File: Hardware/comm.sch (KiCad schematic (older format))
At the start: 0 parts

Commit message: reassigned pin to correct I2C1, I2C2, and USART1 connections
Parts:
- added C?: CP_Small, symbol CP_Small
- added P?: CONN_01X06, symbol CONN_01X06
- added P?: GROVE_OUTPUT_2MM, symbol CONN_01X04
- added P?: GROVE_INPUT_2MM, symbol CONN_01X04
- added P?: BOOT, symbol CONN_01X03
- added R? (x5): 0, symbol R_Small
- added SW?: SW_Push, symbol SW_Push
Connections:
- net labels added: BOOT0, GND, NRST, PWR, SCL, SDA, SWCLK, SWDIO, TRACE
- wire segments 0 -> 31
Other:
- note added: "NOTE: TRACE is reserved and not connected"
- note added: "RESET BUTTON"

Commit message: initial footprint assignments
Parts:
- removed C?: CP_Small, symbol CP_Small
- added C301: 0.1u, Capacitors_SMD:C_0805, symbol C_Small
- P301: renamed from P?; footprint (none) -> Pin_Headers:Pin_Header_Straight_1x06
- P304: renamed from P?; footprint (none) -> Pin_Headers:Pin_Header_Straight_1x03
- R301, R302, R303, R304, R305: renamed from R?; footprint (none) -> Resistors_SMD:R_0805
- gave numbers to parts that had none: 3
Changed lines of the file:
@@
 $EndDescr
 $Comp
-L CONN_01X06 P?
+L CONN_01X06 P301
 U 1 1 58DF9C44
 P 4515 1295
-F 0 "P?" H 4515 1645 50  0000 C CNN
+F 0 "P301" H 4515 1645 50  0000 C CNN
 F 1 "CONN_01X06" V 4615 1295 50  0000 C CNN
-F 2 "" H 4515 1295 50  0000 C CNN
+F 2 "Pin_Headers:Pin_Header_Straight_1x06" H 4515 1295 50  0001 C CNN
 F 3 "" H 4515 1295 50  0000 C CNN
 	1    4515 1295
@@
 $EndComp
 $Comp
-L R_Small R?
+L R_Small R301
 U 1 1 58DF9D23
 P 4085 1045
-F 0 "R?" H 4115 1065 50  0000 L CNN
+F 0 "R301" H 4115 1065 50  0000 L CNN
 F 1 "0" H 4115 1005 50  0000 L CNN
-F 2 "" H 4085 1045 50  0000 C CNN
+F 2 "Resistors_SMD:R_0805" H 4085 1045 50  0001 C CNN
 F 3 "" H 4085 1045 50  0000 C CNN
 F 4 "Value" H 4085 1045 60  0001 C CNN "Fieldname"
@@
 SWCLK
 $Comp
-L GND #PWR?
+L GND #PWR020
 U 1 1 58DF9E37
 P 2955 1245
-F 0 "#PWR?" H 2955 995 50  0001 C CNN
+F 0 "#PWR020" H 2955 995 50  0001 C CNN
 F 1 "GND" H 2955 1095 50  0000 C CNN
 F 2 "" H 2955 1245 50  0000 C CNN
@@
 NOTE: TRACE is reserved and not connected
 $Comp
-L CONN_01X04 P?
+L CONN_01X04 P302
 U 1 1 58E0FECE
 P 7910 1290
-F 0 "P?" H 7910 1540 50  0000 C CNN
+F 0 "P302" H 7910 1540 50  0000 C CNN
 F 1 "GROVE_OUTPUT_2MM" V 8010 1290 50  0000 C CNN
-F 2 "" H 7910 1290 50  0000 C CNN
+F 2 "" H 7910 1290 50  0001 C CNN
 F 3 "" H 7910 1290 50  0000 C CNN
 F 4 "Value" H 7910 1290 60  0001 C CNN "Fieldname"
@@
 PWR
 $Comp
-L GND #PWR?
+L GND #PWR021
 U 1 1 58E10BA0
 P 6750 1140
-F 0 "#PWR?" H 6750 890 50  0001 C CNN
+F 0 "#PWR021" H 6750 890 50  0001 C CNN
 F 1 "GND" H 6750 990 50  0000 C CNN
 F 2 "" H 6750 1140 50  0000 C CNN
@@
 SDA
 $Comp
-L CONN_01X04 P?
+L CONN_01X04 P303
 U 1 1 58E10C1E
 P 7910 2220
-F 0 "P?" H 7910 2470 50  0000 C CNN
+F 0 "P303" H 7910 2470 50  0000 C CNN
 F 1 "GROVE_INPUT_2MM" V 8010 2220 50  0000 C CNN
-F 2 "" H 7910 2220 50  0000 C CNN
+F 2 "" H 7910 2220 50  0001 C CNN
 F 3 "" H 7910 2220 50  0000 C CNN
 F 4 "Value" H 7910 2220 60  0001 C CNN "Fieldname"
@@
 $EndComp
 $Comp
-L R_Small R?
+L R_Small R305
 U 1 1 58E10C90
 P 7640 1760
-F 0 "R?" H 7670 1780 50  0000 L CNN
+F 0 "R305" H 7670 1780 50  0000 L CNN
 F 1 "0" H 7615 1765 50  0000 L CNN
-F 2 "" H 7640 1760 50  0000 C CNN
+F 2 "Resistors_SMD:R_0805" H 7640 1760 50  0001 C CNN
 F 3 "" H 7640 1760 50  0000 C CNN
 F 4 "Value" H 7640 1760 60  0001 C CNN "Fieldname"
@@
 $EndComp
 $Comp
-L R_Small R?
+L R_Small R304
 U 1 1 58E10CC8
 P 7550 1760
-F 0 "R?" H 7555 1875 50  0000 L CNN
+F 0 "R304" H 7555 1875 50  0000 L CNN
 F 1 "0" H 7530 1760 50  0000 L CNN
-F 2 "" H 7550 1760 50  0000 C CNN
+F 2 "Resistors_SMD:R_0805" H 7550 1760 50  0001 C CNN
 F 3 "" H 7550 1760 50  0000 C CNN
 F 4 "Value" H 7550 1760 60  0001 C CNN "Fieldname"
@@
 $EndComp
 $Comp
-L R_Small R?
+L R_Small R303
 U 1 1 58E10CF9
 P 7450 1760
-F 0 "R?" H 7455 1880 50  0000 L CNN
+F 0 "R303" H 7455 1880 50  0000 L CNN
 F 1 "0" H 7430 1760 50  0000 L CNN
-F 2 "" H 7450 1760 50  0000 C CNN
+F 2 "Resistors_SMD:R_0805" H 7450 1760 50  0001 C CNN
 F 3 "" H 7450 1760 50  0000 C CNN
 F 4 "Value" H 7450 1760 60  0001 C CNN "Fieldname"
@@
 $EndComp
 $Comp
-L R_Small R?
+L R_Small R302
 U 1 1 58E10D31
 P 7350 1760
-F 0 "R?" H 7200 1795 50  0000 L CNN
+F 0 "R302" H 7200 1795 50  0000 L CNN
 F 1 "0" H 7330 1760 50  0000 L CNN
-F 2 "" H 7350 1760 50  0000 C CNN
+F 2 "Resistors_SMD:R_0805" H 7350 1760 50  0001 C CNN
 F 3 "" H 7350 1760 50  0000 C CNN
 F 4 "Value" H 7350 1760 60  0001 C CNN "Fieldname"
@@
 $EndComp
 $Comp
-L SW_Push SW?
+L SW_Push SW301
 U 1 1 58E13285
 P 5620 3800
-F 0 "SW?" H 5670 3900 50  0000 L CNN
+F 0 "SW301" H 5670 3900 50  0000 L CNN
 F 1 "SW_Push" H 5620 3740 50  0000 C CNN
-F 2 "" H 5620 4000 50  0000 C CNN
+F 2 "" H 5620 4000 50  0001 C CNN
 F 3 "" H 5620 4000 50  0000 C CNN
 	1    5620 3800
@@
 $EndComp
 $Comp
-L CP_Small C?
-U 1 1 58E132D2
-P 5625 4050
-F 0 "C?" H 5635 4120 50  0000 L CNN
-F 1 "CP_Small" H 5635 3970 50  0000 L CNN
-F 2 "" H 5625 4050 50  0000 C CNN
-F 3 "" H 5625 4050 50  0000 C CNN
-	1    5625 4050
-	0    1    1    0
-$EndComp
-$Comp
-L GND #PWR?
+L GND #PWR022
 U 1 1 58E1344F
 P 5820 4145
-F 0 "#PWR?" H 5820 3895 50  0001 C CNN
+F 0 "#PWR022" H 5820 3895 50  0001 C CNN
 F 1 "GND" H 5820 3995 50  0000 C CNN
 F 2 "" H 5820 4145 50  0000 C CNN
@@
 RESET BUTTON
 $Comp
-L CONN_01X03 P?
+L CONN_01X03 P304
 U 1 1 58E182A5
 P 9270 4480
-F 0 "P?" H 9270 4680 50  0000 C CNN
+F 0 "P304" H 9270 4680 50  0000 C CNN
 F 1 "BOOT" V 9370 4480 50  0000 C CNN
-F 2 "" H 9270 4480 50  0000 C CNN
+F 2 "Pin_Headers:Pin_Header_Straight_1x03" H 9270 4480 50  0001 C CNN
 F 3 "" H 9270 4480 50  0000 C CNN
 F 4 "Value" H 9270 4480 60  0001 C CNN "Fieldname"
@@
 PWR
 $Comp
-L GND #PWR?
+L GND #PWR023
 U 1 1 58E18682
 P 8540 4580
-F 0 "#PWR?" H 8540 4330 50  0001 C CNN
+F 0 "#PWR023" H 8540 4330 50  0001 C CNN
 F 1 "GND" H 8540 4430 50  0000 C CNN
 F 2 "" H 8540 4580 50  0000 C CNN
@@
 Text HLabel 8540 4480 0    60   Input ~ 0
 BOOT0
+$Comp
+L C_Small C301
+U 1 1 58E1A7F8
+P 5625 4050
+F 0 "C301" H 5635 4120 50  0000 L CNN
+F 1 "0.1u" H 5635 3970 50  0000 L CNN
+F 2 "Capacitors_SMD:C_0805" H 5625 4050 50  0001 C CNN
+F 3 "" H 5625 4050 50  0000 C CNN
+F 4 "Value" H 5625 4050 60  0001 C CNN "Fieldname"
+	1    5625 4050
+	0    1    1    0
+$EndComp
 $EndSCHEMATC

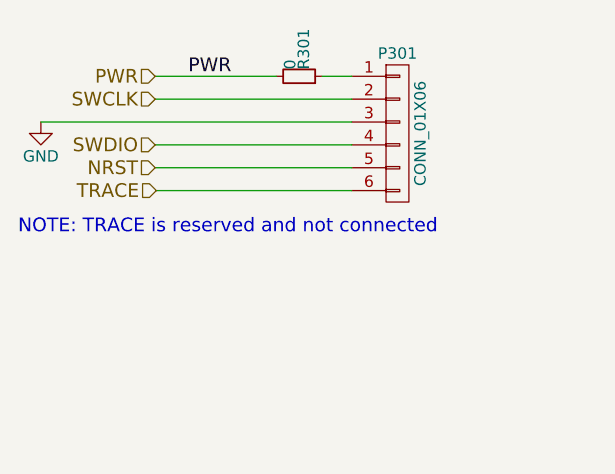
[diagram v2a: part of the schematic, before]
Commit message: added crystal details and usb footprint
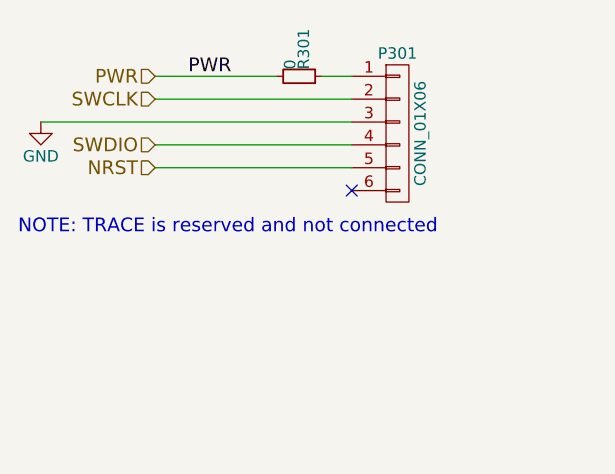
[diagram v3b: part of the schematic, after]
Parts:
- P302, P303: footprint (none) -> Connectors_JST:JST_PH_B4B-PH-K_04x2.00mm_Straight
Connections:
- net TRACE: no longer names the net of P301.6 (P6)
- no-connect marks 0 -> 1
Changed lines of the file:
@@
 SWCLK
 $Comp
-L GND #PWR020
+L GND #PWR022
 U 1 1 58DF9E37
 P 2955 1245
-F 0 "#PWR020" H 2955 995 50  0001 C CNN
+F 0 "#PWR022" H 2955 995 50  0001 C CNN
 F 1 "GND" H 2955 1095 50  0000 C CNN
 F 2 "" H 2955 1245 50  0000 C CNN
@@
 Text HLabel 3455 1445 0    60   Input ~ 0
 NRST
-Text HLabel 3460 1545 0    60   Input ~ 0
-TRACE
 Text Notes 2855 1740 0    60   ~ 0
 NOTE: TRACE is reserved and not connected
@@
 F 0 "P302" H 7910 1540 50  0000 C CNN
 F 1 "GROVE_OUTPUT_2MM" V 8010 1290 50  0000 C CNN
-F 2 "" H 7910 1290 50  0001 C CNN
+F 2 "Connectors_JST:JST_PH_B4B-PH-K_04x2.00mm_Straight" H 7910 1290 50  0001 C CNN
 F 3 "" H 7910 1290 50  0000 C CNN
 F 4 "Value" H 7910 1290 60  0001 C CNN "Fieldname"
@@
 PWR
 $Comp
-L GND #PWR021
+L GND #PWR023
 U 1 1 58E10BA0
 P 6750 1140
-F 0 "#PWR021" H 6750 890 50  0001 C CNN
+F 0 "#PWR023" H 6750 890 50  0001 C CNN
 F 1 "GND" H 6750 990 50  0000 C CNN
 F 2 "" H 6750 1140 50  0000 C CNN
@@
 F 0 "P303" H 7910 2470 50  0000 C CNN
 F 1 "GROVE_INPUT_2MM" V 8010 2220 50  0000 C CNN
-F 2 "" H 7910 2220 50  0001 C CNN
+F 2 "Connectors_JST:JST_PH_B4B-PH-K_04x2.00mm_Straight" H 7910 2220 50  0001 C CNN
 F 3 "" H 7910 2220 50  0000 C CNN
 F 4 "Value" H 7910 2220 60  0001 C CNN "Fieldname"
@@
 $EndComp
 $Comp
-L GND #PWR022
+L GND #PWR024
 U 1 1 58E1344F
 P 5820 4145
-F 0 "#PWR022" H 5820 3895 50  0001 C CNN
+F 0 "#PWR024" H 5820 3895 50  0001 C CNN
 F 1 "GND" H 5820 3995 50  0000 C CNN
 F 2 "" H 5820 4145 50  0000 C CNN
@@
 	4315 1345 3455 1345
 Wire Wire Line
-	4315 1545 3460 1545
-Wire Wire Line
 	6750 1140 7710 1140
 Wire Wire Line
@@
 PWR
 $Comp
-L GND #PWR023
+L GND #PWR025
 U 1 1 58E18682
 P 8540 4580
-F 0 "#PWR023" H 8540 4330 50  0001 C CNN
+F 0 "#PWR025" H 8540 4330 50  0001 C CNN
 F 1 "GND" H 8540 4430 50  0000 C CNN
 F 2 "" H 8540 4580 50  0000 C CNN
@@
 	0    1    1    0
 $EndComp
+NoConn ~ 4315 1545
 $EndSCHEMATC

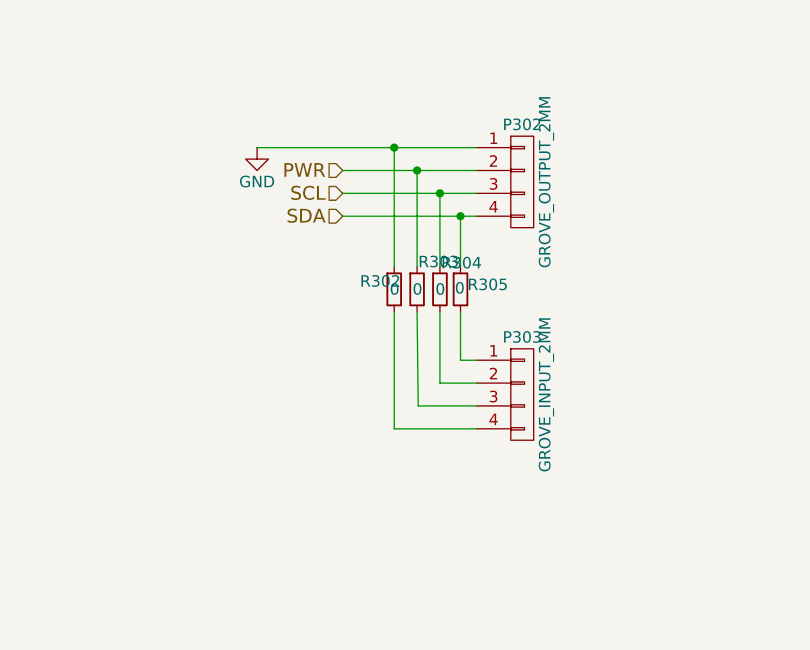
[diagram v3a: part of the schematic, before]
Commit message: changed grove connectors to jst sh and added VCC and GND to other headers
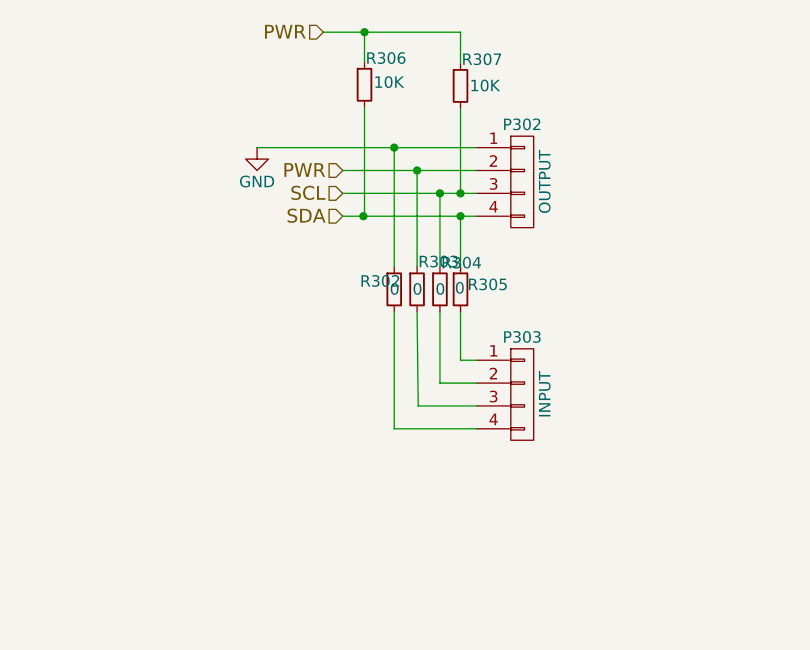
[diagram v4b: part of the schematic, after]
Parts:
- added R306, R307: 10K, Resistors_SMD:R_0805, symbol R_Small
- P302: value GROVE_OUTPUT_2MM -> OUTPUT; footprint Connectors_JST:JST_PH_B4B-PH-K_04x2.00mm_Straight -> Connectors_JST:JST_SH_BM04B-SRSS-TB_04x1.00mm_Straight; Fieldname Value -> (none); MPN (none) -> BM04B-SRSS-TB(LF)(SN)
- P303: value GROVE_INPUT_2MM -> INPUT; footprint Connectors_JST:JST_PH_B4B-PH-K_04x2.00mm_Straight -> Connectors_JST:JST_SH_BM04B-SRSS-TB_04x1.00mm_Straight; MPN (none) -> BM04B-SRSS-TB(LF)(SN)
- SW301: MPN (none) -> TL3315NF100Q
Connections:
- net PWR: now also R306.1, R307.1
- net SCL: now also R307.2
- net SDA: now also R306.2
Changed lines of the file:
@@
 SWCLK
 $Comp
-L GND #PWR022
+L GND #PWR019
 U 1 1 58DF9E37
 P 2955 1245
-F 0 "#PWR022" H 2955 995 50  0001 C CNN
+F 0 "#PWR019" H 2955 995 50  0001 C CNN
 F 1 "GND" H 2955 1095 50  0000 C CNN
 F 2 "" H 2955 1245 50  0000 C CNN
@@
 P 7910 1290
 F 0 "P302" H 7910 1540 50  0000 C CNN
-F 1 "GROVE_OUTPUT_2MM" V 8010 1290 50  0000 C CNN
-F 2 "Connectors_JST:JST_PH_B4B-PH-K_04x2.00mm_Straight" H 7910 1290 50  0001 C CNN
-F 3 "" H 7910 1290 50  0000 C CNN
-F 4 "Value" H 7910 1290 60  0001 C CNN "Fieldname"
+F 1 "OUTPUT" V 8010 1290 50  0000 C CNN
+F 2 "Connectors_JST:JST_SH_BM04B-SRSS-TB_04x1.00mm_Straight" H 7910 1290 50  0001 C CNN
+F 3 "http://www.jst-mfg.com/product/pdf/eng/eSH.pdf" H 7910 1290 50  0001 C CNN
+F 4 "BM04B-SRSS-TB(LF)(SN)" H 7910 1290 60  0001 C CNN "MPN"
 	1    7910 1290
 	1    0    0    -1
@@
 PWR
 $Comp
-L GND #PWR023
+L GND #PWR020
 U 1 1 58E10BA0
 P 6750 1140
-F 0 "#PWR023" H 6750 890 50  0001 C CNN
+F 0 "#PWR020" H 6750 890 50  0001 C CNN
 F 1 "GND" H 6750 990 50  0000 C CNN
 F 2 "" H 6750 1140 50  0000 C CNN
@@
 Text HLabel 7125 1440 0    60   Input ~ 0
 SDA
-$Comp
-L CONN_01X04 P303
-U 1 1 58E10C1E
-P 7910 2220
-F 0 "P303" H 7910 2470 50  0000 C CNN
-F 1 "GROVE_INPUT_2MM" V 8010 2220 50  0000 C CNN
-F 2 "Connectors_JST:JST_PH_B4B-PH-K_04x2.00mm_Straight" H 7910 2220 50  0001 C CNN
-F 3 "" H 7910 2220 50  0000 C CNN
-F 4 "Value" H 7910 2220 60  0001 C CNN "Fieldname"
-	1    7910 2220
-	1    0    0    -1
-$EndComp
 $Comp
 L R_Small R305
@@
 F 1 "SW_Push" H 5620 3740 50  0000 C CNN
 F 2 "" H 5620 4000 50  0001 C CNN
-F 3 "" H 5620 4000 50  0000 C CNN
+F 3 "https://media.digikey.com/pdf/Data%20Sheets/E-Switch%20PDFs/TL3315.pdf" H 5620 4000 50  0001 C CNN
+F 4 "TL3315NF100Q" H 5620 3800 60  0001 C CNN "MPN"
 	1    5620 3800
 	1    0    0    -1
 $EndComp
 $Comp
-L GND #PWR024
+L GND #PWR021
 U 1 1 58E1344F
 P 5820 4145
-F 0 "#PWR024" H 5820 3895 50  0001 C CNN
+F 0 "#PWR021" H 5820 3895 50  0001 C CNN
 F 1 "GND" H 5820 3995 50  0000 C CNN
 F 2 "" H 5820 4145 50  0000 C CNN
@@
 PWR
 $Comp
-L GND #PWR025
+L GND #PWR022
 U 1 1 58E18682
 P 8540 4580
-F 0 "#PWR025" H 8540 4330 50  0001 C CNN
+F 0 "#PWR022" H 8540 4330 50  0001 C CNN
 F 1 "GND" H 8540 4430 50  0000 C CNN
 F 2 "" H 8540 4580 50  0000 C CNN
@@
 $EndComp
 NoConn ~ 4315 1545
+$Comp
+L R_Small R306
+U 1 1 58E300D6
+P 7220 865
+F 0 "R306" H 7225 980 50  0000 L CNN
+F 1 "10K" H 7260 875 50  0000 L CNN
+F 2 "Resistors_SMD:R_0805" H 7220 865 50  0001 C CNN
+F 3 "" H 7220 865 50  0000 C CNN
+F 4 "Value" H 7220 865 60  0001 C CNN "Fieldname"
+	1    7220 865
+	1    0    0    -1
+$EndComp
+$Comp
+L R_Small R307
+U 1 1 58E30137
+P 7640 870
+F 0 "R307" H 7645 985 50  0000 L CNN
+F 1 "10K" H 7680 870 50  0000 L CNN
+F 2 "Resistors_SMD:R_0805" H 7640 870 50  0001 C CNN
+F 3 "" H 7640 870 50  0000 C CNN
+F 4 "Value" H 7640 870 60  0001 C CNN "Fieldname"
+	1    7640 870
+	1    0    0    -1
+$EndComp
+Wire Wire Line
+	7640 970  7640 1340
+Connection ~ 7640 1340
+Wire Wire Line
+	7220 965  7220 1440
+Wire Wire Line
+	7220 1440 7215 1440
+Connection ~ 7215 1440
+Text HLabel 7040 635  0    60   Input ~ 0
+PWR
+Wire Wire Line
+	7040 635  7640 635
+Wire Wire Line
+	7640 635  7640 770
+Wire Wire Line
+	7220 765  7220 635
+Connection ~ 7220 635
+$Comp
+L CONN_01X04 P303
+U 1 1 58E91128
+P 7910 2220
+F 0 "P303" H 7910 2470 50  0000 C CNN
+F 1 "INPUT" V 8010 2220 50  0000 C CNN
+F 2 "Connectors_JST:JST_SH_BM04B-SRSS-TB_04x1.00mm_Straight" H 7910 2220 50  0001 C CNN
+F 3 "http://www.jst-mfg.com/product/pdf/eng/eSH.pdf" H 7910 2220 50  0001 C CNN
+F 4 "Value" H 7910 2220 60  0001 C CNN "Fieldname"
+F 5 "BM04B-SRSS-TB(LF)(SN)" H 7910 2220 60  0001 C CNN "MPN"
+	1    7910 2220
+	1    0    0    -1
+$EndComp
 $EndSCHEMATC

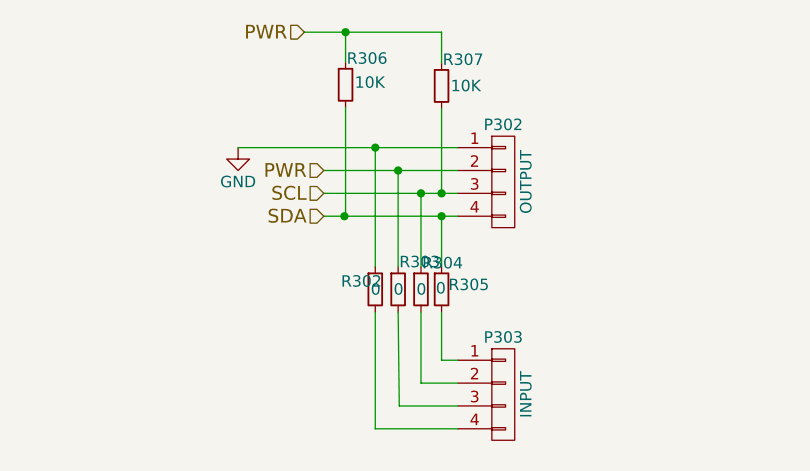
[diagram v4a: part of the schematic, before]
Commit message: fixed jst sh headers and added button footprint
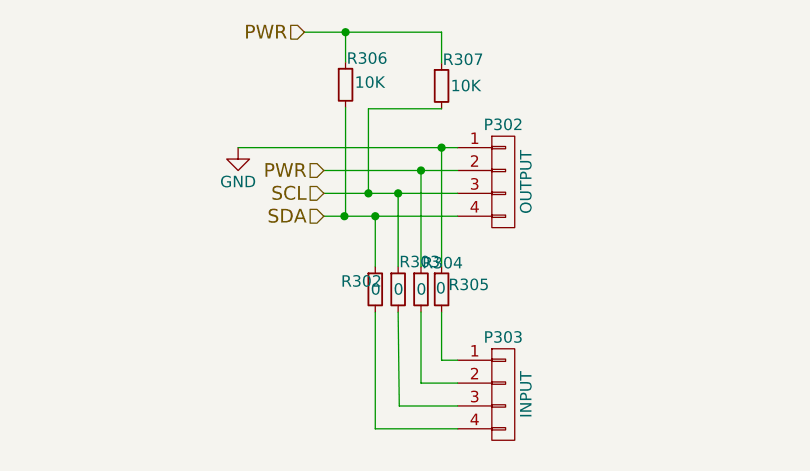
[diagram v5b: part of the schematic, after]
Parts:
- SW301: footprint (none) -> CentralCommand:TL3315
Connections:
- net GND: now also R305.1; no longer R302.1
- net PWR: now also R304.1; no longer R303.1
- net SCL: now also R303.1; no longer R304.1
- net SDA: now also R302.1; no longer R305.1
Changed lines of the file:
@@
 SWCLK
 $Comp
-L GND #PWR019
+L GND #PWR020
 U 1 1 58DF9E37
 P 2955 1245
-F 0 "#PWR019" H 2955 995 50  0001 C CNN
+F 0 "#PWR020" H 2955 995 50  0001 C CNN
 F 1 "GND" H 2955 1095 50  0000 C CNN
 F 2 "" H 2955 1245 50  0000 C CNN
@@
 PWR
 $Comp
-L GND #PWR020
+L GND #PWR021
 U 1 1 58E10BA0
 P 6750 1140
-F 0 "#PWR020" H 6750 890 50  0001 C CNN
+F 0 "#PWR021" H 6750 890 50  0001 C CNN
 F 1 "GND" H 6750 990 50  0000 C CNN
 F 2 "" H 6750 1140 50  0000 C CNN
@@
 F 0 "SW301" H 5670 3900 50  0000 L CNN
 F 1 "SW_Push" H 5620 3740 50  0000 C CNN
-F 2 "" H 5620 4000 50  0001 C CNN
+F 2 "CentralCommand:TL3315" H 5620 4000 50  0001 C CNN
 F 3 "https://media.digikey.com/pdf/Data%20Sheets/E-Switch%20PDFs/TL3315.pdf" H 5620 4000 50  0001 C CNN
 F 4 "TL3315NF100Q" H 5620 3800 60  0001 C CNN "MPN"
@@
 $EndComp
 $Comp
-L GND #PWR021
+L GND #PWR022
 U 1 1 58E1344F
 P 5820 4145
-F 0 "#PWR021" H 5820 3895 50  0001 C CNN
+F 0 "#PWR022" H 5820 3895 50  0001 C CNN
 F 1 "GND" H 5820 3995 50  0000 C CNN
 F 2 "" H 5820 4145 50  0000 C CNN
@@
 	6750 1140 7710 1140
 Wire Wire Line
-	7125 1240 7710 1240
-Wire Wire Line
 	7125 1340 7710 1340
 Wire Wire Line
@@
 	7640 2070 7640 1860
 Wire Wire Line
-	7640 1660 7640 1440
-Connection ~ 7640 1440
-Wire Wire Line
 	7550 2170 7710 2170
 Wire Wire Line
 	7550 1860 7550 2170
 Wire Wire Line
-	7550 1660 7550 1340
-Connection ~ 7550 1340
-Wire Wire Line
-	7450 1240 7450 1660
-Wire Wire Line
-	7445 1240 7450 1240
-Wire Wire Line
-	7350 1660 7350 1140
-Connection ~ 7350 1140
-Wire Wire Line
 	7350 1860 7350 2370
 Wire Wire Line
@@
 Wire Wire Line
 	7450 1860 7455 2270
-Connection ~ 7450 1240
 Wire Wire Line
 	5420 3800 5420 4050
@@
 PWR
 $Comp
-L GND #PWR022
+L GND #PWR023
 U 1 1 58E18682
 P 8540 4580
-F 0 "#PWR022" H 8540 4330 50  0001 C CNN
+F 0 "#PWR023" H 8540 4330 50  0001 C CNN
 F 1 "GND" H 8540 4430 50  0000 C CNN
 F 2 "" H 8540 4580 50  0000 C CNN
@@
 $EndComp
 Wire Wire Line
-	7640 970  7640 1340
-Connection ~ 7640 1340
-Wire Wire Line
 	7220 965  7220 1440
 Wire Wire Line
@@
 	1    0    0    -1
 $EndComp
+Wire Wire Line
+	7125 1240 7710 1240
+Wire Wire Line
+	7640 1660 7640 1140
+Connection ~ 7640 1140
+Wire Wire Line
+	7550 1660 7550 1240
+Connection ~ 7550 1240
+Wire Wire Line
+	7450 1660 7450 1340
+Connection ~ 7450 1340
+Wire Wire Line
+	7350 1440 7350 1660
+Connection ~ 7350 1440
+Wire Wire Line
+	7640 970  7320 970
+Wire Wire Line
+	7320 970  7320 1340
+Connection ~ 7320 1340
 $EndSCHEMATC

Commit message: started board layout
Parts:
- P301: value CONN_01X06 -> PROGRAM; Fieldname (none) -> Value
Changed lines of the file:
@@
 P 4515 1295
 F 0 "P301" H 4515 1645 50  0000 C CNN
-F 1 "CONN_01X06" V 4615 1295 50  0000 C CNN
+F 1 "PROGRAM" V 4615 1295 50  0000 C CNN
 F 2 "Pin_Headers:Pin_Header_Straight_1x06" H 4515 1295 50  0001 C CNN
 F 3 "" H 4515 1295 50  0000 C CNN
+F 4 "Value" H 4515 1295 60  0001 C CNN "Fieldname"
 	1    4515 1295
 	1    0    0    -1
